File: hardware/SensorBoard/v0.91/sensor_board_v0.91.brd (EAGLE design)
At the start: 52.5 x 43 mm, 46 parts, among them IC1 BMP280, IC2 VREF, J3 USB-MICROB, U1 LMP91000, U10 CCS811, U11 RFM69HW, U2 TSL2561, U3 ATMEGA328P-MU, U4 ADS1115, U7 SHT31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

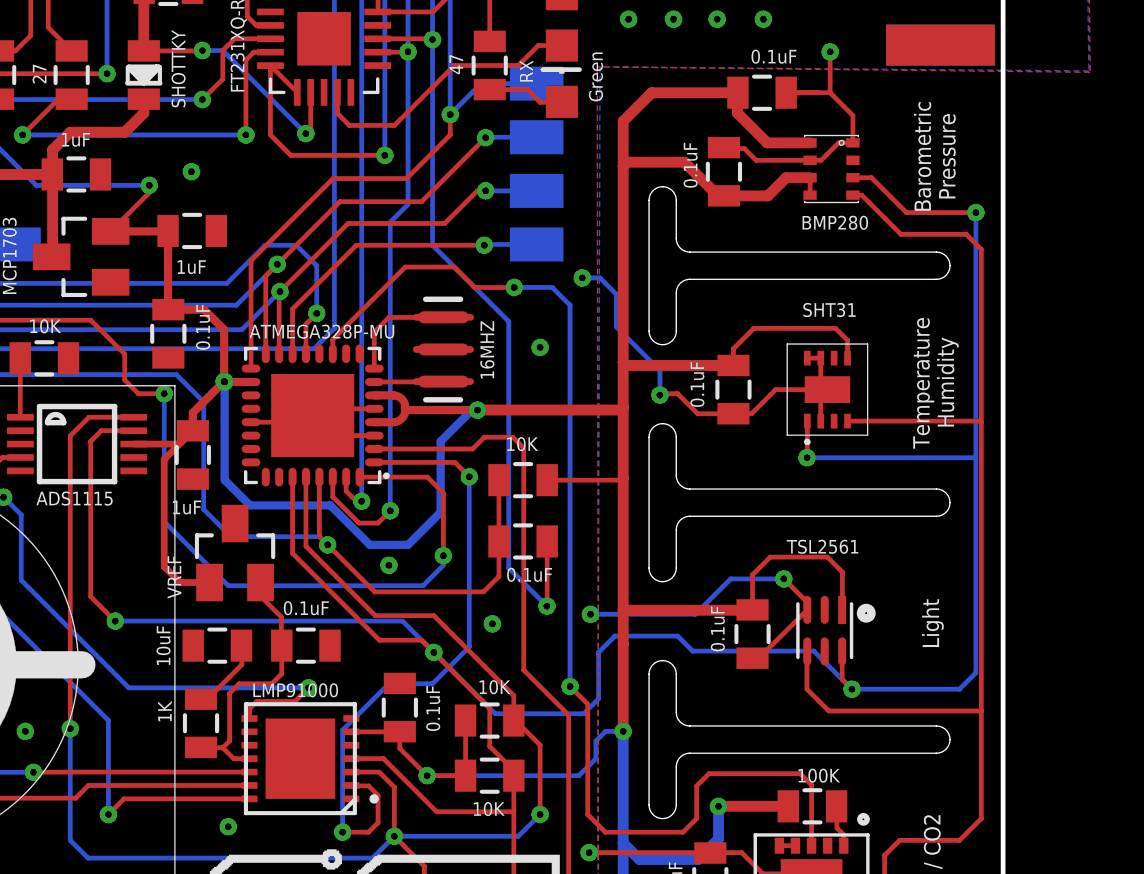
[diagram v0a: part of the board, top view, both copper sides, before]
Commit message: Updated SHT31 library
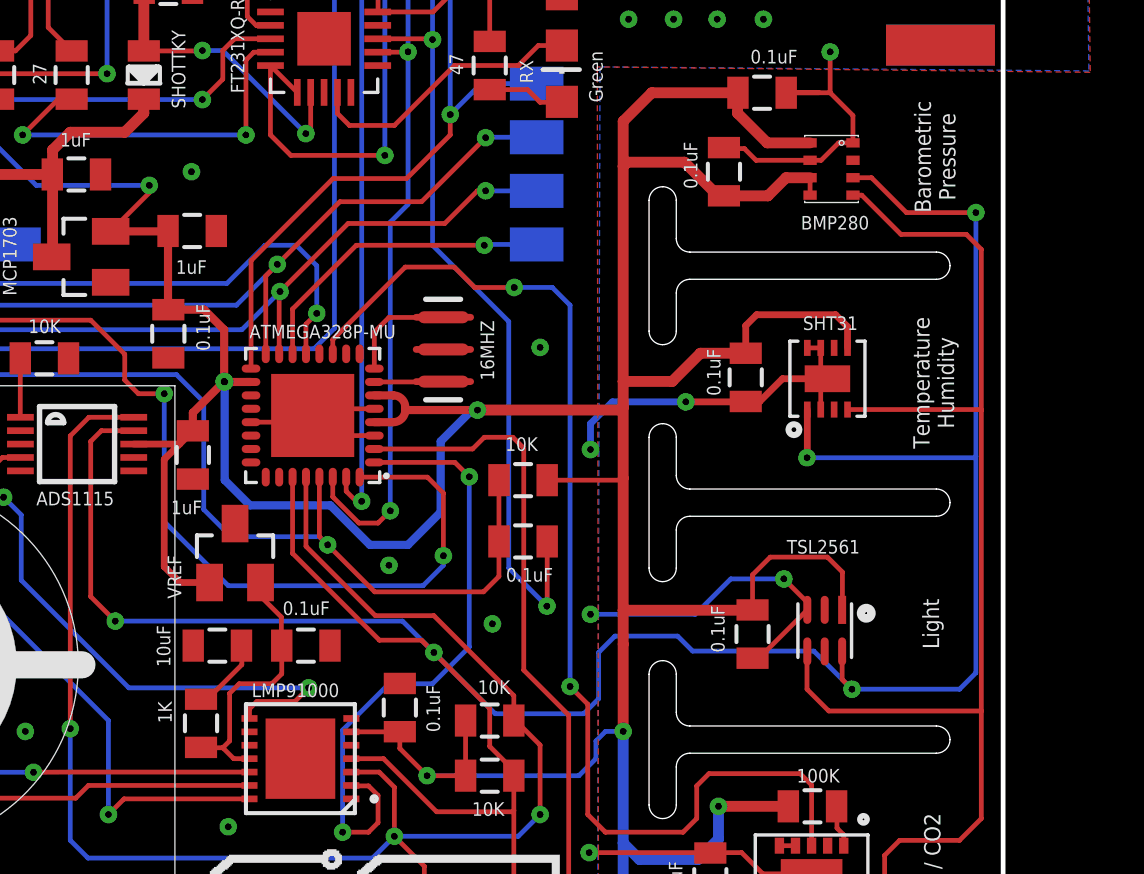
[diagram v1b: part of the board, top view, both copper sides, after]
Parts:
- removed C4: 0.1uF, SparkFun-Passives:0805
- removed U7: SHT31, thomasb9511:SHT3X
- added C14: 0.1uF, SparkFun-Passives:0805
- added U5: SHT31, SHT31:SHT3X
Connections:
- net GND: now also C14.2, U5.2, U5.7, U5.8, U5.THERMAL; no longer C4.2, U7.P$2, U7.P$7, U7.P$8, U7.PAD
- net SCL: now also U5.4; no longer U7.P$4
- net SDA: now also U5.1; no longer U7.P$1
- net VCC: now also C14.1, U5.5; no longer C4.1, U7.P$5
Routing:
- net GND: track 56.0 -> 53.6 mm
- net VCC: track 171.9 -> 172.5 mm

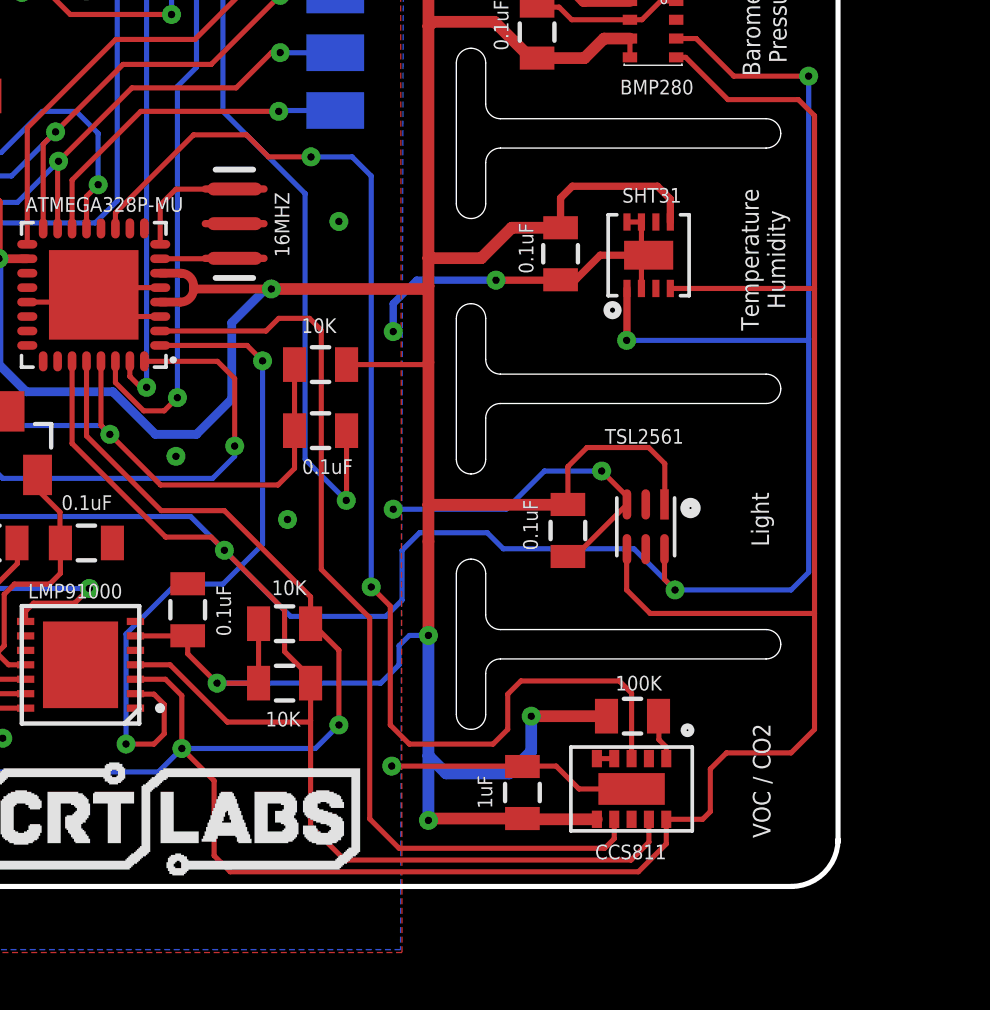
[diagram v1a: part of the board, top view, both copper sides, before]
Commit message: Design update
Replaced TSL2561 with TSL2591 sensor
Rearranged a few traces around the CCS811 sensor
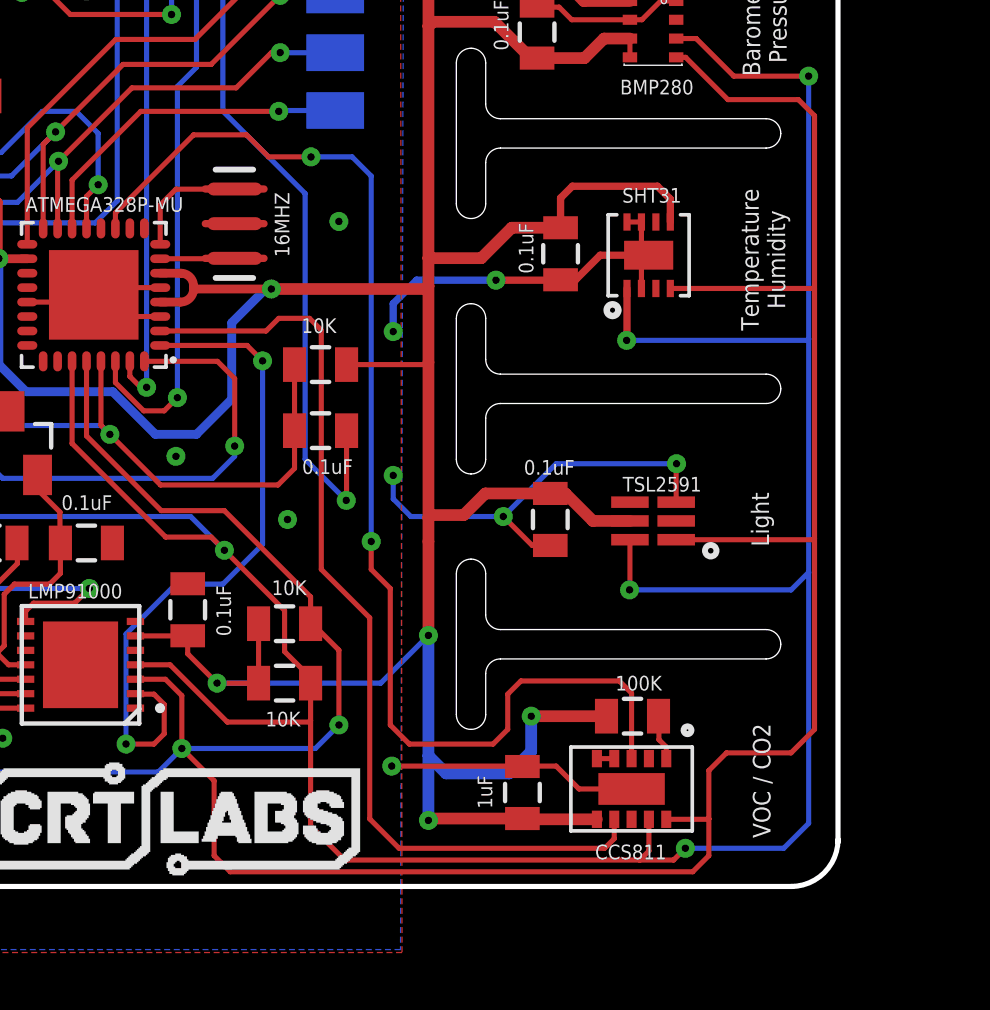
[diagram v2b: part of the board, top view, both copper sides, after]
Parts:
- removed C3: 0.1uF, SparkFun-Passives:0805
- removed U2: TSL2561, SparkFun-DigitalIC:FN-6
- added C4: 0.1uF, SparkFun-Passives:0805
- added U6: TSL2591, TSL2591:DFN6_TAOS
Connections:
- net GND: now also C4.2, U6.3; no longer C3.2, U2.3
- net SCL: now also U6.1; no longer U2.4
- net SDA: now also U6.6; no longer U2.6
- net VCC: now also C4.1, U6.5; no longer C3.1, U2.1
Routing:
- net VCC: track 172.5 -> 168.4 mm
- net GND: track 53.6 -> 56.5 mm, vias 33 -> 34
- net SDA: track 118.2 -> 115.6 mm, vias 5 -> 6
- net SCL: track 126.1 -> 124.5 mm
